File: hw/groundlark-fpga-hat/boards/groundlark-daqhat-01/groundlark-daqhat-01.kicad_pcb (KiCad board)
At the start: 6 copper layers, 85 x 56 mm, 128 parts, among them J1 Raspberry Pi 40-pin, J4 FPGA test UART/reset, J80 LSHM-150-04.0-L-DV-A-S-K-TR, J81 LSHM-150-04.0-L-DV-A-S-K-TR, J82 LSHM-130-04.0-L-DV-A-S-K-TR, J83 1715721, J90 GEO + / - / SHIELD, Q1 2N7002, U1 24LC32A, U100 TMUX1574PWR, U101 TMUX1574PWR, U102 TCA9534PWR, U103 SN74LVC1G10DCKR, U104 TLV809EA30DBZR, U105 TLV809EA30DBZR, U106 SN74LVC1G08DCKR, U11 LSM6DSOTR, U12 LSM6DSOTR, U13 LSM6DSOTR, U22 ADS122C04, U40 TLV1117LV33DCYR, U41 SN74LVC8T245PWR, U42 SN74LVC8T245PWR, U43 ISO1640BDR, U51 TXU0202DCUR, U52 TLV803EA30DBZR

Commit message: Harden Groundlark and Skylark acquisition, power checks and assembly
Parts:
- moved C43 5.50 mm to (129.2, 88.7)
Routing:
- net GND: track 654.3 -> 657.8 mm, vias 67 -> 76
- net SENS_3V3: track 235.7 -> 237.9 mm
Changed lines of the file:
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@@
 		)
 		(embedded_fonts no)
-		(model "${KIPRJMOD}/../../../shared/models/Pi_ESQ_120_23.wrl"
+		(model "${KIPRJMOD}/../../../shared/models/Pi_Megastar_2x20.wrl"
 			(offset
 				(xyz 0 0 0)
@@
 	(footprint "Groundlark:Capacitor_SMD__C_0603_1608Metric"
 		(layer "F.Cu")
-		(at 124 90.5)
+		(at 129.199999 88.7)
 		(descr "Capacitor SMD 0603 (1608 Metric), square (rectangular) end terminal, IPC-7351 nominal, (Body size source: IPC-SM-782 page 76, https://www.pcb-3d.com/wordpress/wp-content/uploads/ipc-sm-782a_amendment_1_and_2.pdf), generated with kicad-footprint-generator")
 		(tags "capacitor")
@@
 	)
 	(segment
-		(start 122.9185 90.1935)
-		(end 123.225 90.5)
-		(width 1.2)
-		(layer "F.Cu")
-		(net 51)
-	)
-	(segment
 		(start 90.2 82.525)
 		(end 90.225 82.5)
@@
 	)
 	(segment
-		(start 122.9185 89.2924)
-		(end 122.9185 90.1935)
-		(width 1.2)
-		(layer "F.Cu")
-		(net 51)
-	)
-	(segment
 		(start 71.775 74.65)
 		(end 71.75 74.65)
@@
 	)
 	(segment
+		(start 126.15 86)
+		(end 128.424999 88.7)
+		(width 0.2)
+		(layer "F.Cu")
+		(net 51)
+	)
+	(segment
 		(start 91.5 72)
 		(end 91.5 71.95)
@@
 	)
 	(segment
+		(start 112.8625 76.575)
+		(end 113.2 77)
+		(width 0.2)
+		(layer "F.Cu")
+		(net 145)
+	)
+	(segment
 		(start 75.7 88.8)
 		(end 75.725 88.8)
@@
 	)
 	(segment
+		(start 129.974999 88.7)
+		(end 130 88.7)
+		(width 0.2)
+		(layer "F.Cu")
+		(net 145)
+	)
+	(segment
 		(start 57.05 94.3)
 		(end 61.15 94.3)
@@
 	)
 	(segment
+		(start 112.8625 88.575)
+		(end 113.65 88.9)
+		(width 0.2)
+		(layer "F.Cu")
+		(net 145)
+	)
+	(segment
 		(start 112.8625 87.275)
 		(end 112.8625 87.925)
@@
 	)
 	(segment
+		(start 107.1375 88.575)
+		(end 106.3 88.6)
+		(width 0.2)
+		(layer "F.Cu")
+		(net 145)
+	)
+	(segment
 		(start 116.1975 74.685)
 		(end 116.1975 67.4225)
@@
 	)
 	(segment
+		(start 56.95 89.5)
+		(end 57.6 89.5)
+		(width 0.2)
+		(layer "F.Cu")
+		(net 145)
+	)
+	(segment
 		(start 61.8375 85.75)
 		(end 61.5492 85.75)
@@
 	)
 	(segment
+		(start 55.95 97)
+		(end 56.6 97)
+		(width 0.2)
+		(layer "F.Cu")
+		(net 145)
+	)
+	(segment
 		(start 110.75 95.85)
 		(end 110.75 94.8733)
@@
 	)
 	(via
+		(at 124.775 81)
+		(size 0.45)
+		(drill 0.3)
+		(layers "F.Cu" "B.Cu")
+		(net 145)
+	)
+	(via
 		(at 78.775 94.5)
 		(size 0.45)
@@
 	)
 	(via
+		(at 57.6 89.5)
+		(size 0.45)
+		(drill 0.3)
+		(layers "F.Cu" "B.Cu")
+		(net 145)
+	)
+	(via
 		(at 78 79.7)
 		(size 0.45)
@@
 	)
 	(via
+		(at 113.2 77)
+		(size 0.45)
+		(drill 0.3)
+		(layers "F.Cu" "B.Cu")
+		(net 145)
+	)
+	(via
 		(at 64.95 88.15)
 		(size 0.45)
@@
 	)
 	(via
+		(at 130 88.7)
+		(size 0.45)
+		(drill 0.3)
+		(layers "F.Cu" "B.Cu")
+		(net 145)
+	)
+	(via
 		(at 75.85 88.675)
 		(size 0.45)
@@
 	)
 	(via
+		(at 56.6 97)
+		(size 0.45)
+		(drill 0.3)
+		(layers "F.Cu" "B.Cu")
+		(net 145)
+	)
+	(via
 		(at 73.1 69.7)
 		(size 0.45)
@@
 	)
 	(via
+		(at 113.65 88.9)
+		(size 0.45)
+		(drill 0.3)
+		(layers "F.Cu" "B.Cu")
+		(net 145)
+	)
+	(via
 		(at 60.6 91.5)
 		(size 0.45)
@@
 	)
 	(via
+		(at 106.3 88.6)
+		(size 0.45)
+		(drill 0.3)
+		(layers "F.Cu" "B.Cu")
+		(net 145)
+	)
+	(via
 		(at 61.1375 93.675)
 		(size 0.45)
@@
 	)
 	(via
+		(at 117 86.525)
+		(size 0.45)
+		(drill 0.3)
+		(layers "F.Cu" "B.Cu")
+		(net 145)
+	)
+	(via
 		(at 63.2 76.2)
 		(size 0.45)
@@
 		(net 145)
 	)
+	(via
+		(at 120 79.05)
+		(size 0.45)
+		(drill 0.3)
+		(layers "F.Cu" "B.Cu")
+		(net 145)
+	)

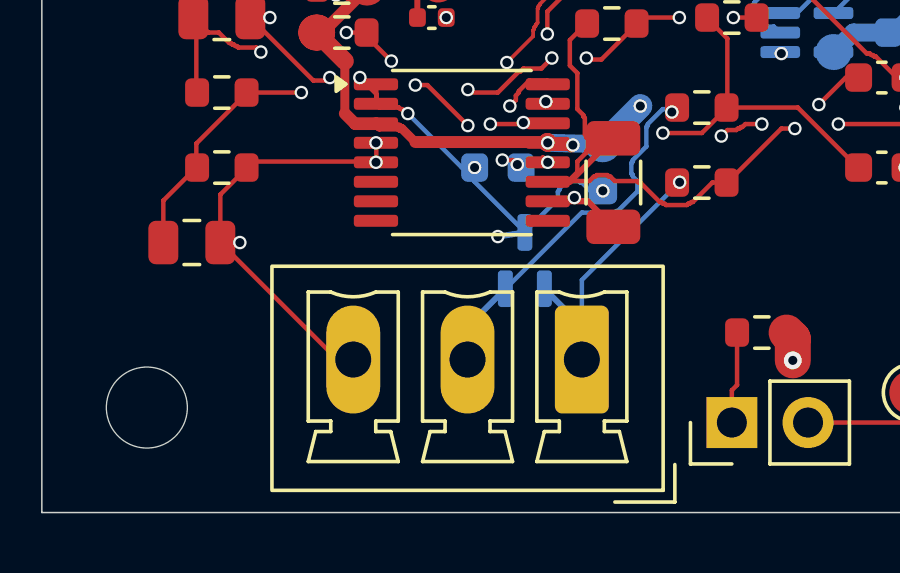
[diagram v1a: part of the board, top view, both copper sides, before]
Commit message: Use horizontal geophone connector and publish detailed enclosure render
Synchronize J90 routing, native SES, assembly mapping, enclosure fit, models and validation. Add a 4K clear-PETG README render and derive assembly PDF part identities from package procurement. Preserve Git-normalized source bindings and original validation/render input hashes. Generated JLCPCB packages remain local.
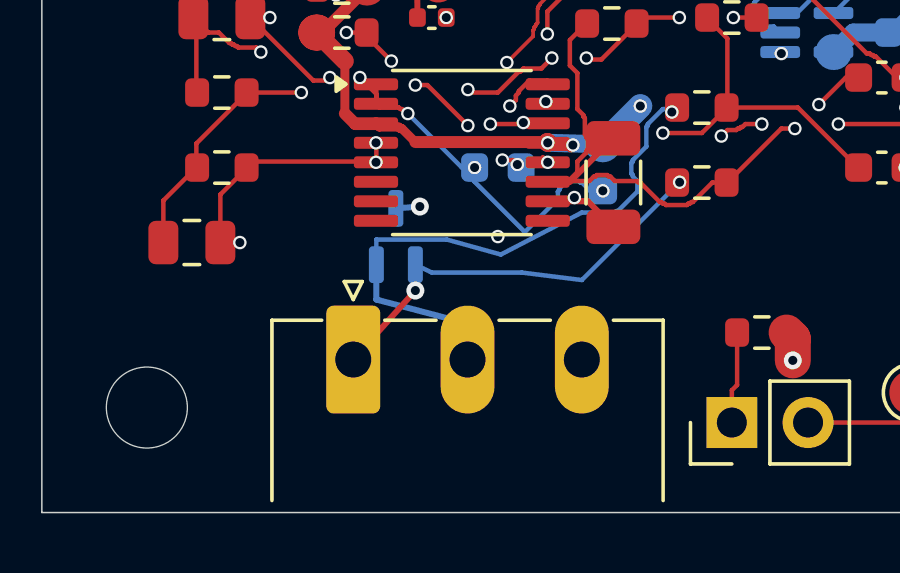
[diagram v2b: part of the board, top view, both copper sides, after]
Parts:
- J90: footprint Groundlark:Connector_Phoenix_MC__PhoenixContact_MCV_1,5_3-G-3.81_1x03_P3.81mm_Vertical -> Groundlark:Connector_Phoenix_MC__PhoenixContact_MC_1,5_3-G-3.81_1x03_P3.81mm_Horizontal
- moved J90 7.62 mm to (60.4, 100.9), turned to 0 degrees
- moved D90 4.37 mm to (61.8, 96.8)
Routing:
- net GND: track 657.8 -> 651.6 mm, vias 76 -> 77
- net GEO_N: track 14.3 -> 19.6 mm
- net GEO_P: track 9.19 -> 14.3 mm, vias 1 -> 2

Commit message: Add TI Pi power supervision and expand DAQHAT enclosure
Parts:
- added C110: 22u, Groundlark:PWR_C_1210_3225Metric, F.Cu at (141.0, 88.0)
- added C111: 22u, Groundlark:PWR_C_1210_3225Metric, F.Cu at (146.0, 88.0)
- added C112: 22u, Groundlark:PWR_C_1210_3225Metric, F.Cu at (151.0, 89.0)
- added C130: 4.7u, Groundlark:SUP_C_0805_2012Metric, F.Cu at (162.0, 86.0)
- added C131: 10u, Groundlark:PWR_C_1206_3216Metric, F.Cu at (161.0, 77.0)
- added C132: 10u, Groundlark:PWR_C_1206_3216Metric, F.Cu at (170.0, 73.0)
- added C133: 10u, Groundlark:PWR_C_1206_3216Metric, F.Cu at (178.0, 73.0)
- added C134: 100n, Groundlark:PWR_C_0603_1608Metric, F.Cu at (174.0, 74.0)
- added C135: 47u, Groundlark:PWR_CP_Elec_6.3x7.7, F.Cu at (185.0, 77.0)
- added C136: 22u, Groundlark:PWR_C_1210_3225Metric, F.Cu at (169.0, 84.0)
- added C137: 22u, Groundlark:PWR_C_1210_3225Metric, F.Cu at (174.0, 84.0)
- added C138: 22u, Groundlark:PWR_C_1210_3225Metric, F.Cu at (179.0, 85.0)
- added C139: 10n, Groundlark:SUP_C_0603_1608Metric, F.Cu at (185.0, 90.0)
- added C140: 10u, Groundlark:SUP_C_0805_2012Metric, F.Cu at (188.0, 84.0)
- added C141: 100n, Groundlark:PWR_C_0603_1608Metric, F.Cu at (167.5, 93.5)
- added C142: 10u, Groundlark:SUP_C_0805_2012Metric, F.Cu at (164.5, 93.0)
- added C143: 470n, Groundlark:SUP_C_0603_1608Metric, F.Cu at (170.0, 89.5)
- added C144: 10n, Groundlark:SUP_C_0603_1608Metric, F.Cu at (164.0, 89.0)
- added C145: 10n, Groundlark:SUP_C_0603_1608Metric, F.Cu at (173.5, 88.0)
- added C24: 100n, Groundlark:Capacitor_SMD__C_0603_1608Metric, B.Cu at (54.5, 78.5)
- added C86: 10u, Groundlark:PWR_C_1206_3216Metric, F.Cu at (141.0, 77.0)
- added C87: 10u, Groundlark:PWR_C_1206_3216Metric, F.Cu at (149.0, 77.0)
- added C88: 100n, Groundlark:PWR_C_0603_1608Metric, F.Cu at (145.0, 78.0)
- added C89: 47u, Groundlark:PWR_CP_Elec_6.3x7.7, F.Cu at (155.0, 95.0)
- added D130: B340A, Groundlark:PWR_D_SMA, F.Cu at (170.0, 69.0)
- added D131: SMAJ18A, Groundlark:SUP_D_SMA, F.Cu at (185.0, 68.0)
- added D80: B340A, Groundlark:PWR_D_SMA, F.Cu at (145.0, 71.0)
- added D81: SMAJ15A, Groundlark:PWR_D_SMA, F.Cu at (154.0, 73.0)
- added F130: 4A fast, Groundlark:SUP_Fuse_1206_3216Metric, F.Cu at (163.0, 66.0)
- added J130: PI BATTERY 8-18V, Groundlark:SUP_PhoenixContact_MC_1,5_2-G-3.81_1x02_P3.81mm_Horizontal, F.Cu at (170.0, 60.0)
- added J131: SWD / 3V3 REF, Groundlark:SUP_PinHeader_1x05_P1.27mm_Vertical, F.Cu at (184.0, 95.0)
- added JP130: BENCH RUN, Groundlark:SUP_PinHeader_1x02_P2.54mm_Vertical, F.Cu at (167.0, 102.0)
- added Q130: 2N7002, Groundlark:SUP_SOT-23, F.Cu at (162.0, 98.0)
- added Q131: 2N7002, Groundlark:SUP_SOT-23, F.Cu at (178.0, 96.0)
- added R120: 10k, Groundlark:PWR_R_0603_1608Metric, F.Cu at (150.0, 84.0)
- added R121: 4.30k, Groundlark:PWR_R_0603_1608Metric, F.Cu at (150.0, 81.0)
- added R122: 100k, Groundlark:PWR_R_0603_1608Metric, F.Cu at (137.0, 77.0)
- added R123: 15k, Groundlark:PWR_R_0603_1608Metric, F.Cu at (137.0, 80.0)
- added R124: 10k, Groundlark:PWR_R_0603_1608Metric, F.Cu at (139.5, 84.0)
- added R130: 10k, Groundlark:PWR_R_0603_1608Metric, F.Cu at (179.0, 80.0)
- added R131: 2.41k, Groundlark:SUP_R_0603_1608Metric, F.Cu at (179.0, 77.0)
- added R132: 100k, Groundlark:PWR_R_0603_1608Metric, F.Cu at (166.0, 77.0)
- added R133: 2k, Groundlark:SUP_R_0603_1608Metric, F.Cu at (187.0, 92.0)
- added R134: 47k, Groundlark:SUP_R_0603_1608Metric, F.Cu at (166.5, 90.0)
- added R135: 1M, Groundlark:SUP_R_0603_1608Metric, F.Cu at (180.0, 90.0)
- added R136: 150k, Groundlark:SUP_R_0603_1608Metric, F.Cu at (177.0, 90.0)
- added R137: 100k, Groundlark:PWR_R_0603_1608Metric, F.Cu at (163.0, 101.0)
- added R138: 10k, Groundlark:PWR_R_0603_1608Metric, F.Cu at (159.0, 101.0)
- added R139: 100k, Groundlark:PWR_R_0603_1608Metric, F.Cu at (178.0, 99.0)
- added R140: 100k, Groundlark:PWR_R_0603_1608Metric, F.Cu at (178.0, 93.0)
- added R141: 10k, Groundlark:PWR_R_0603_1608Metric, F.Cu at (168.0, 98.0)
- added SW80: FPGA OFF / ON, Groundlark:PWR_SW_SPDT_PCM12, F.Cu at (155.0, 60.0)
- added U130: MSPM0L1105, Groundlark:SUP_QFN-32-1EP_5x5mm_P0.5mm_EP3.45x3.45mm, F.Cu at (172.0, 94.0)
- added U131: TPS70933, Groundlark:SUP_SOT-23-5, F.Cu at (163.0, 82.0)
- added U132: TPSM53603, Groundlark:PWR_Texas_B3QFN-14-1EP_5x5.5mm_P0.65mm, F.Cu at (174.0, 78.0)
- added U133: TPS22953, Groundlark:SUP_Texas_WSON10_DQC0010A, F.Cu at (184.0, 86.0)
- added U23: DLVR-F50D, Groundlark:Groundlark__DLVR_E1BS, F.Cu at (51.5, 76.0)
- added U80: TPSM53603, Groundlark:PWR_Texas_B3QFN-14-1EP_5x5.5mm_P0.65mm, F.Cu at (145.0, 82.0)
- F80: value 0467005.NR -> 2A fast; footprint Groundlark:TZ_TZ_FUSE -> Groundlark:PWR_Fuse_1206_3216Metric
- J83: value 1715721 -> 12V DC / CENTER +; footprint Groundlark:TZ_TZ_POWER -> Groundlark:PWR_BarrelJack_CUI_PJ-102AH_Horizontal
- moved J83 90.3 mm to (145.0, 64.1), turned to 180 degrees
- moved F80 72.6 mm to (139.0, 68.0)
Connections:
- net EXT_3V3 renamed EXT_12V
- F80 pad 2: FPGA_VIN -> FUSED_12V
- J1 pad 31: 31 -> PI_SHUTDOWN_N
- J1 pad 33: 33 -> PI_HALTED
- J81 pad 31: j81-31 -> 31
- J81 pad 33: j81-33 -> 33
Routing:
- net PI_5V: track 108.4 -> 490.2 mm, vias 4 -> 12
- net PI_HALTED: track 0.00 -> 110.2 mm, vias 0 -> 4
- net PI_SHUTDOWN_N: track 0.00 -> 89.8 mm, vias 0 -> 6
- net BAT_PROTECTED: track 0.00 -> 64.4 mm, vias 0 -> 2
- net PROTECTED_12V: track 0.00 -> 63.9 mm, vias 0 -> 2
- net SUP_RUN: track 0.00 -> 56.4 mm, vias 0 -> 4
- net BUCK_EN: track 0.00 -> 51.4 mm, vias 0 -> 2
- net SUP_3V3: track 0.00 -> 50.9 mm, vias 0 -> 4
- net PI_3V3: track 237.5 -> 287.2 mm, vias 18 -> 20
- net FPGA_EN1: track 25.0 -> 73.9 mm, vias 1 -> 2
- net BAT_FUSED: track 0.00 -> 36.4 mm, vias 0 -> 2
- net PI_RAW_5V: track 0.00 -> 28.1 mm, vias 0 -> 12
- net SUP_NRST: track 0.00 -> 26.9 mm, vias 0 -> 1
- net FPGA_VIN: track 119.8 -> 95.2 mm, vias 12 -> 17
- net I2C_SDA: track 47.1 -> 68.7 mm, vias 12 -> 14
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- added copper zone on F.Cu, net GND
- added copper zone on B.Cu, net PI_RAW_5V
- added copper zone on F.Cu, net PI_RAW_5V
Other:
- board size 85 x 56 mm -> 140 x 56 mm
- board text added: "+ GND"
- board text added: "12V DC / CENTER +"
- board text added: "FPGA ON/OFF"
- board text added: "FPGA POWER"
- board text added: "PI BAT 8-18V"
- board text removed: "3V3 ONLY"
